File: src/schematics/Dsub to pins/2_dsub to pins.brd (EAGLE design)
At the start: 110.5 x 65.5 mm, 32 parts, among them X1 22-23-2021, X10 22-23-2021, X11 22-23-2021, X12 22-23-2021, X13 22-23-2021, X14 22-23-2021, X15 22-23-2021, X16 22-23-2021, X17 22-23-2021, X18 22-23-2021, X19 22-23-2021, X2 22-23-2021, X20 22-23-2021, X21 22-23-2021, X22 22-23-2021, X23 22-23-2021, X24 22-23-2021, X25 22-23-2021, X26 22-23-2021, X27 22-23-2021, X28 22-23-2021, X29 22-23-2021, X3 22-23-2021, X30 22-23-2021, X4 22-23-2021, X5 22-23-2021, X6 22-23-2021, X7 22-23-2021, X8 22-23-2021, X9 22-23-2021

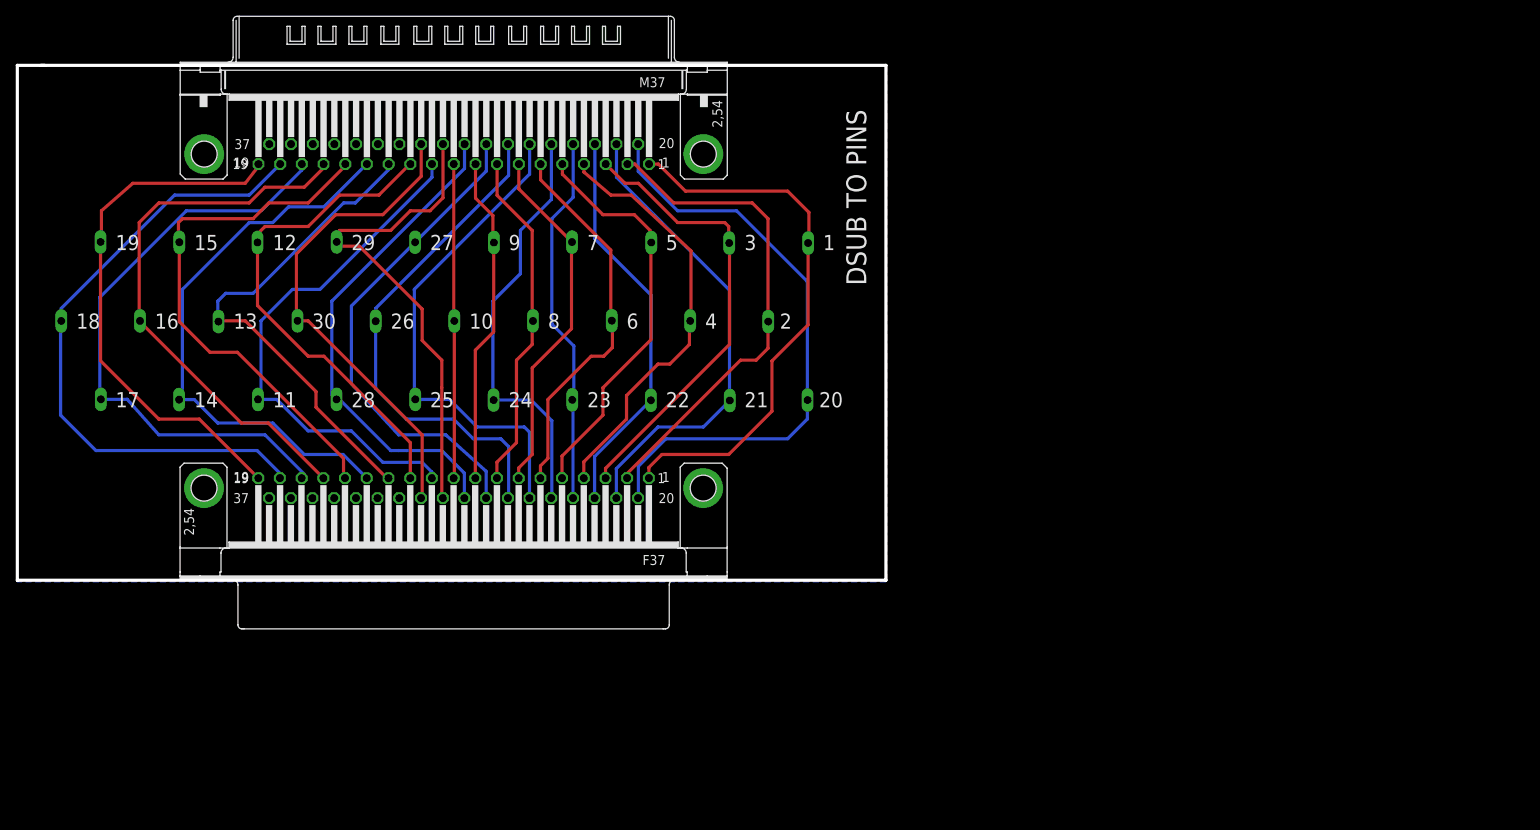
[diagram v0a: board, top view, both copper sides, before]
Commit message: Added schematic changes from summation subtraction branch
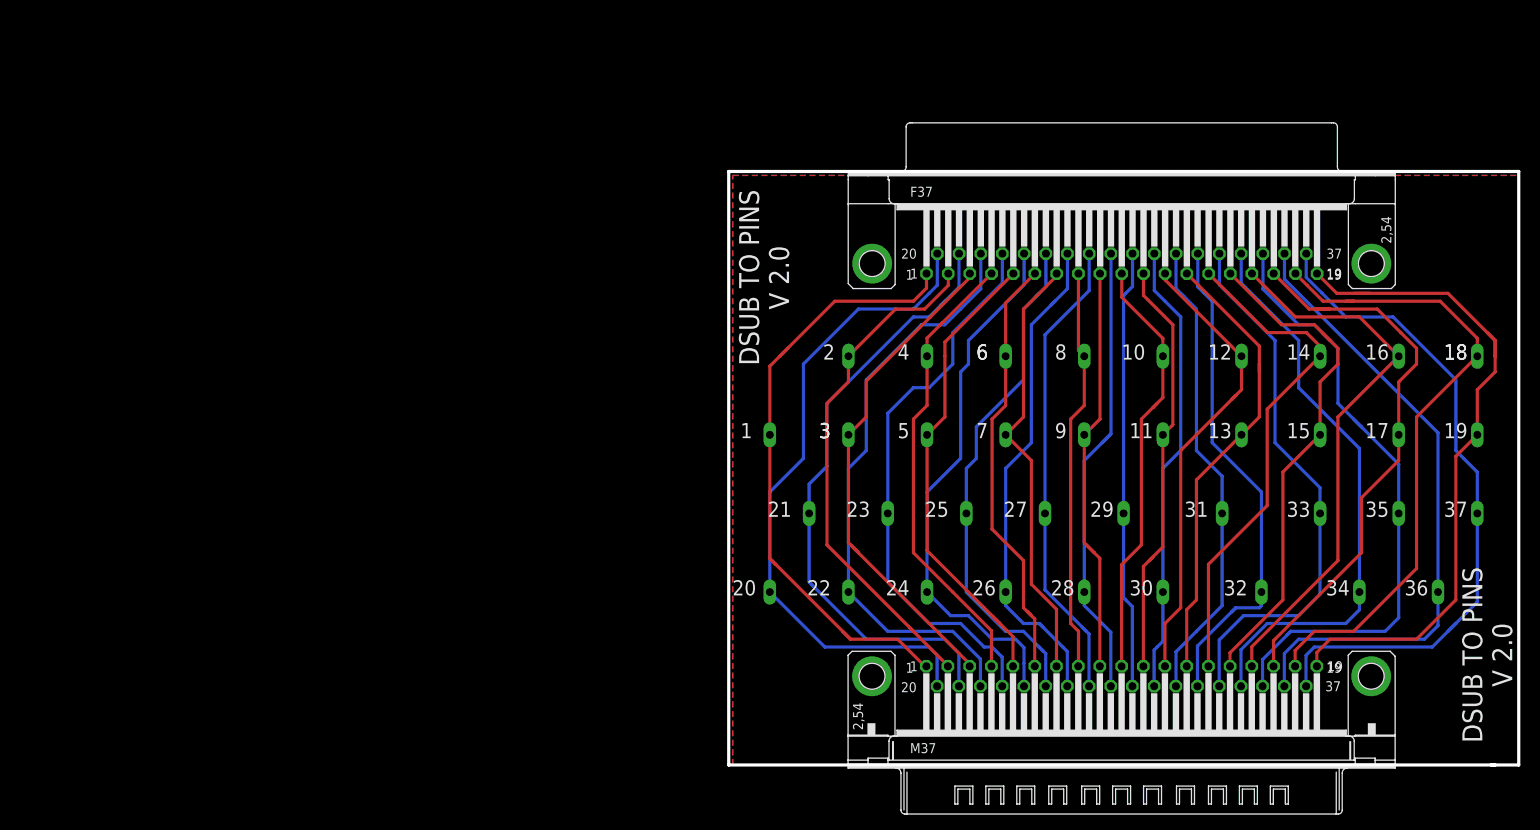
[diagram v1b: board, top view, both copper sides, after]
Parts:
- added X31, X32, X35, X36, X37: 22-23-2021, mayo:22-23-2021
- added X40: (no value), con-subd:M37HP
- added X41: (no value), con-subd:F37HP
- X33: value (none) -> 22-23-2021; device con-subd:M37HP -> mayo:22-23-2021
- X34: value (none) -> 22-23-2021; device con-subd:F37HP -> mayo:22-23-2021
- moved X18 182.7 mm to (45.0, 19.0), turned to 0 degrees
- moved X19 179.4 mm to (45.0, 9.00), turned to 0 degrees
- moved X17 167.7 mm to (35.0, 9.00), turned to 0 degrees
- moved X16 162.7 mm to (35.0, 19.0), turned to 0 degrees
- moved X15 149.7 mm to (25.0, 9.00), turned to 0 degrees
- moved X14 147.8 mm to (25.0, 19.0), turned to 0 degrees
- moved X13 133.5 mm to (15.0, 9.00), turned to 0 degrees
- moved X12 128.5 mm to (15.0, 19.0), turned to 0 degrees
- moved X33 120.5 mm to (25.0, -1.00), turned to 0 degrees
- moved X30 117.8 mm to (5.00, -11.0), turned to 0 degrees
- moved X11 117.7 mm to (5.00, 9.00), turned to 0 degrees
- moved X34 117.2 mm to (30.0, -11.0), turned to 0 degrees
- moved X29 108.3 mm to (0.00, -1.00), turned to 0 degrees
- moved X28 100.7 mm to (-5.00, -11.0), turned to 0 degrees
- moved X10 92.8 mm to (5.00, 19.0), turned to 0 degrees
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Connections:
- removed net N$28: X33.32
- removed net N$29: X33.34
- removed net N$30: X33.36
- removed net N$36: X33.31
- removed net N$37: X33.33
- removed net N$38: X33.35
- removed net N$39: X33.37
- removed net N$68: X34.31
- removed net N$69: X34.32
- removed net N$70: X34.33
- removed net N$71: X34.34
- removed net N$72: X34.35
- removed net N$73: X34.36
- removed net N$74: X34.37
- new net 31: X31.1, X40.31, X41.31
- new net 32: X32.1, X40.32, X41.32
- new net 33: X33.1, X40.33, X41.33
- new net 34: X34.1, X40.34, X41.34
- new net 35: X35.1, X40.35, X41.35
- new net 36: X36.1, X40.36, X41.36
- new net 37: X37.1, X40.37, X41.37
- net 1: now also X40.1, X41.1; no longer X33.1, X34.1
- net 10: now also X40.10, X41.10; no longer X33.10, X34.10
- net 11: now also X40.11, X41.11; no longer X33.11, X34.11
- net 12: now also X40.12, X41.12; no longer X33.12, X34.12
- net 13: now also X40.13, X41.13; no longer X33.13, X34.13
- net 14: now also X40.14, X41.14; no longer X33.14, X34.14
- net 15: now also X40.15, X41.15; no longer X33.15, X34.15
- net 16: now also X40.16, X41.16; no longer X33.16, X34.16
- net 17: now also X40.17, X41.17; no longer X33.17, X34.17
- net 18: now also X40.18, X41.18; no longer X33.18, X34.18
- net 19: now also X40.19, X41.19; no longer X33.19, X34.19
- net 2: now also X40.2, X41.2; no longer X33.2, X34.2
- net 20: now also X40.20, X41.20; no longer X33.20, X34.20
- net 21: now also X40.21, X41.21; no longer X33.21, X34.21
- net 22: now also X40.22, X41.22; no longer X33.22, X34.22
- net 23: now also X40.23, X41.23; no longer X33.23, X34.23
- net 24: now also X40.24, X41.24; no longer X33.24, X34.24
- net 25: now also X40.25, X41.25; no longer X33.25, X34.25
- net 26: now also X40.26, X41.26; no longer X33.26, X34.26
- net 27: now also X40.27, X41.27; no longer X33.27, X34.27
- net 28: now also X40.28, X41.28; no longer X33.28, X34.28
- net 29: now also X40.29, X41.29; no longer X33.29, X34.29
- net 3: now also X40.3, X41.3; no longer X33.3, X34.3
- net 30: now also X40.30, X41.30; no longer X33.30, X34.30
- net 4: now also X40.4, X41.4; no longer X33.4, X34.4
- net 5: now also X40.5, X41.5; no longer X33.5, X34.5
- net 6: now also X40.6, X41.6; no longer X33.6, X34.6
- net 7: now also X40.7, X41.7; no longer X33.7, X34.7
- net 8: now also X40.8, X41.8; no longer X33.8, X34.8
- net 9: now also X40.9, X41.9; no longer X33.9, X34.9
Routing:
- net 37: track 0.00 -> 86.8 mm
- net 36: track 0.00 -> 80.6 mm
- net 35: track 0.00 -> 79.7 mm
- net 34: track 0.00 -> 73.4 mm
- net 33: track 0.00 -> 69.8 mm
- net 32: track 0.00 -> 64.2 mm
- net 31: track 0.00 -> 60.6 mm
- net 22: track 51.0 -> 75.6 mm
- net 23: track 47.4 -> 71.2 mm
- net 19: track 68.6 -> 88.9 mm
- net 21: track 60.4 -> 79.3 mm
- net 10: track 40.0 -> 55.0 mm
- net 24: track 54.1 -> 68.3 mm
- net 11: track 67.9 -> 53.8 mm
- net 9: track 41.9 -> 53.0 mm
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- added copper zone on layer 16, net N$1
- added copper zone on layer 1, net N$2
- removed copper zone on layer 1, net N$1
- removed copper zone on layer 16, net N$2
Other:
- board size 110.5 x 65.5 mm -> 100.5 x 75.5 mm
- board text added: "DSUB TO PINS V 2.0"
- board text removed: "DSUB TO PINS"

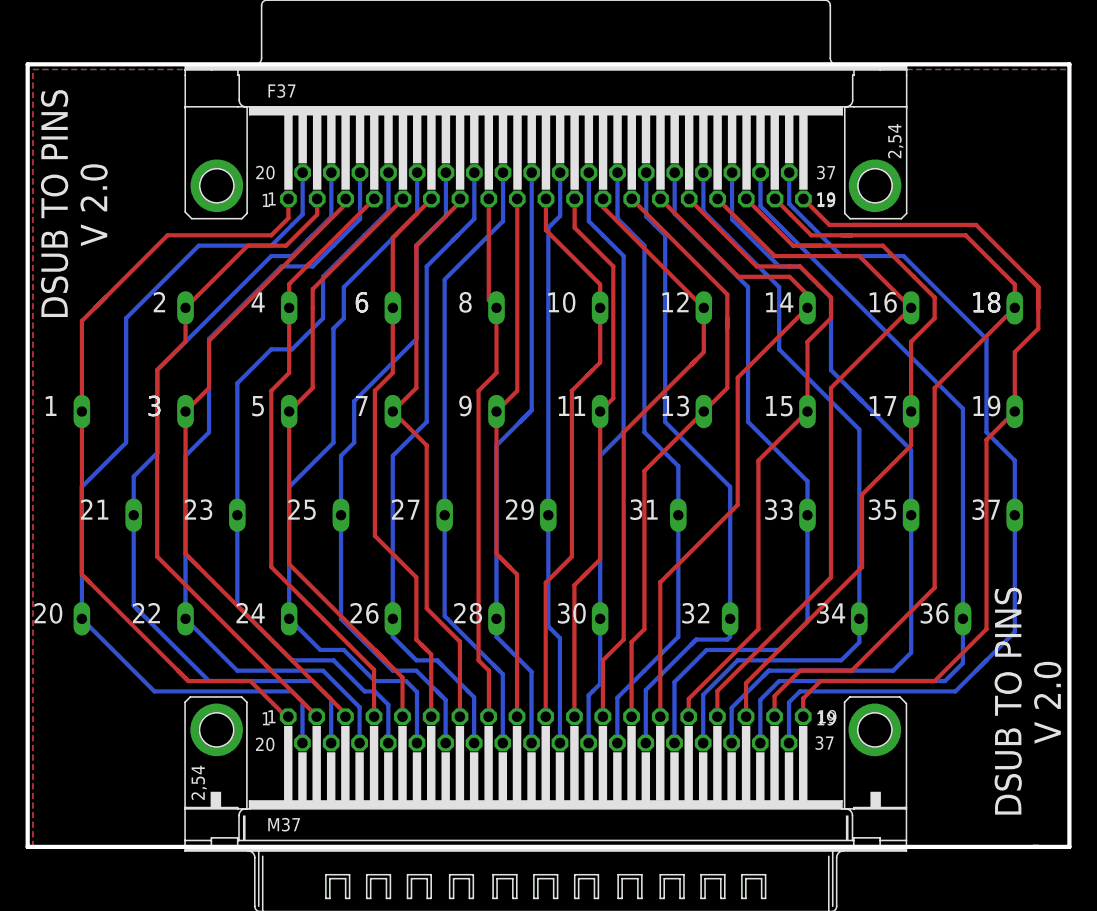
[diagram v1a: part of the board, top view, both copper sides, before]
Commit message: New Debug phantom, and new Dsub adaptors. With Gerbers sent to PCBWay
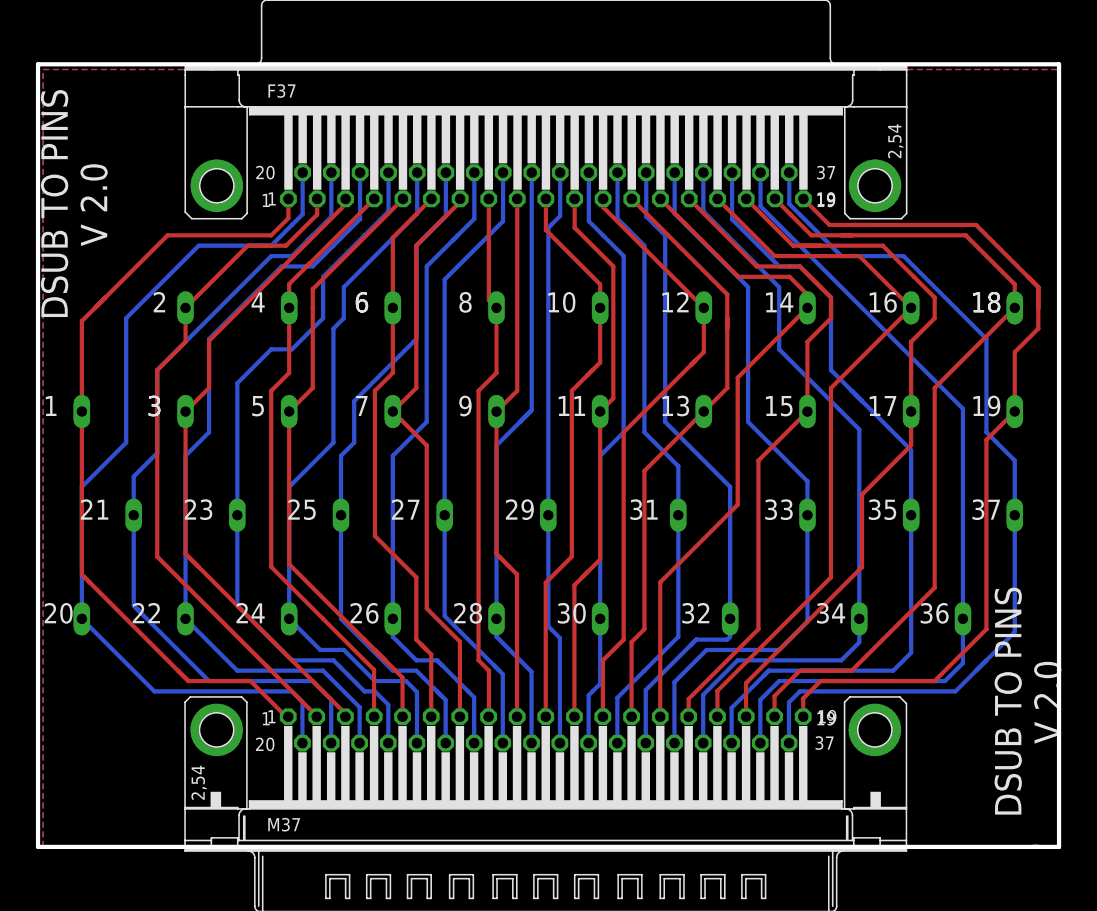
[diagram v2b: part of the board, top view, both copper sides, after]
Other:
- board size 100.5 x 75.5 mm -> 98.5 x 75.5 mm
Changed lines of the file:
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@@
 <layer number="45" name="Holes" color="7" fill="1" visible="no" active="yes"/>
 <layer number="46" name="Milling" color="3" fill="1" visible="no" active="yes"/>
-<layer number="47" name="Measures" color="7" fill="1" visible="no" active="yes"/>
+<layer number="47" name="Measures" color="7" fill="1" visible="yes" active="yes"/>
 <layer number="48" name="Document" color="7" fill="1" visible="no" active="yes"/>
 <layer number="49" name="Reference" color="7" fill="1" visible="no" active="yes"/>
@@
 <text x="42.5" y="20.5" size="1.9304" layer="25" ratio="20" rot="R180">18</text>
 <text x="42.5" y="10.5" size="1.9304" layer="25" ratio="20" rot="R180">19</text>
-<text x="-48" y="-9.5" size="1.9304" layer="25" ratio="20" rot="R180">20</text>
+<text x="-47" y="-9.5" size="1.9304" layer="25" ratio="20" rot="R180">20</text>
 <text x="-43.5" y="0.5" size="1.9304" layer="25" ratio="20" rot="R180">21</text>
 <text x="-38.5" y="-9.5" size="1.9304" layer="25" ratio="20" rot="R180">22</text>
@@
 <text x="19" y="35" size="1.27" layer="26" ratio="20" rot="MR180">36</text>
 <text x="22" y="35" size="1.27" layer="26" ratio="20" rot="MR180">37</text>
-<wire x1="46" y1="-33" x2="-51.5" y2="-33" width="0.4064" layer="20"/>
-<wire x1="-51.5" y1="-33" x2="-51.5" y2="42.5" width="0.4064" layer="20"/>
-<wire x1="-51.5" y1="42.5" x2="49" y2="42.5" width="0.4064" layer="20"/>
-<wire x1="49" y1="42.5" x2="49" y2="-33" width="0.4064" layer="20"/>
-<wire x1="49" y1="-33" x2="45.5" y2="-33" width="0.4064" layer="20"/>
+<wire x1="46" y1="-33" x2="-50.5" y2="-33" width="0.4064" layer="20"/>
+<wire x1="-50.5" y1="-33" x2="-50.5" y2="42.5" width="0.4064" layer="20"/>
+<wire x1="-50.5" y1="42.5" x2="48" y2="42.5" width="0.4064" layer="20"/>
+<wire x1="48" y1="42.5" x2="48" y2="-33" width="0.4064" layer="20"/>
+<wire x1="48" y1="-33" x2="45.5" y2="-33" width="0.4064" layer="20"/>
 <text x="-47" y="29" size="2.54" layer="25" ratio="31" rot="R270" align="center">DSUB TO PINS
 V 2.0</text>
-<dimension x1="-16" y1="8" x2="-126" y2="-30" x3="-71" y3="-22" textsize="1.778" layer="47" dtype="horizontal"/>
-<dimension x1="-126.5" y1="8" x2="-166" y2="74" x3="-170" y3="41" textsize="1.778" layer="47" dtype="vertical"/>
 <text x="14.5" y="-9.5" size="1.9304" layer="25" ratio="20" rot="R180">32</text>
 <text x="27.5" y="-9.5" size="1.9304" layer="25" ratio="20" rot="R180">34</text>
@@
 <text x="29.5" y="0.5" size="1.9304" layer="26" ratio="20" rot="MR180">35</text>
 <text x="39.5" y="0.5" size="1.9304" layer="26" ratio="20" rot="MR180">37</text>
-<text x="-51" y="-9.5" size="1.9304" layer="26" ratio="20" rot="MR180">20</text>
+<text x="-50" y="-9.5" size="1.9304" layer="26" ratio="20" rot="MR180">20</text>
 <text x="-41.5" y="-9.5" size="1.9304" layer="26" ratio="20" rot="MR180">22</text>
 <text x="-31.5" y="-9.5" size="1.9304" layer="26" ratio="20" rot="MR180">24</text>
@@
 <text x="45" y="-19" size="2.54" layer="25" ratio="31" rot="R90" align="center">DSUB TO PINS
 V 2.0</text>
+<dimension x1="-50.5" y1="42.5" x2="48" y2="42.5" x3="-1.25" y3="58" textsize="1.778" layer="47"/>
+<dimension x1="48" y1="42.5" x2="48" y2="-33" x3="67" y3="4.75" textsize="1.778" layer="47"/>
 </plain>
 <attributes>
@@
 <signal name="N$1">
 <polygon width="0.4064" layer="16">
-<vertex x="-51" y="42"/>
-<vertex x="49" y="42"/>
-<vertex x="49" y="-33"/>
-<vertex x="-51" y="-33"/>
+<vertex x="-50" y="42"/>
+<vertex x="48" y="42"/>
+<vertex x="48" y="-33"/>
+<vertex x="-50" y="-33"/>
 </polygon>
 </signal>
 <signal name="N$2">
 <polygon width="0.4064" layer="1">
-<vertex x="-51" y="42"/>
-<vertex x="49" y="42"/>
-<vertex x="49" y="-33"/>
-<vertex x="-51" y="-33"/>
+<vertex x="-50" y="42"/>
+<vertex x="48" y="42"/>
+<vertex x="48" y="-33"/>
+<vertex x="-50" y="-33"/>
 </polygon>
 </signal>
